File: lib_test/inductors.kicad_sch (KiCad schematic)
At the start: 1 part

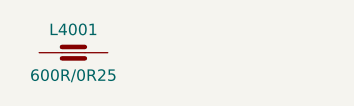
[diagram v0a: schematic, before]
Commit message: Add do not populate parts
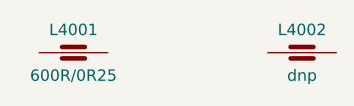
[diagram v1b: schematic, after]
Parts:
- added L4002: dnp, lily_footprints:ind_0805_dnp, symbol lily_symbols:ind_bead_do_not_populate_0805
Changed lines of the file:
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@@
 	(paper "A4")
+	(symbol
+		(lib_id "lily_symbols:ind_bead_do_not_populate_0805")
+		(at 50.8 25.4 0)
+		(unit 1)
+		(exclude_from_sim no)
+		(in_bom yes)
+		(on_board yes)
+		(dnp no)
+		(property "Reference" "L4002"
+			(at 54.61 22.86 0)
+			(effects
+				(font
+					(size 1.27 1.27)
+				)
+			)
+		)
+		(property "Value" "dnp"
+			(at 54.61 27.94 0)
+			(effects
+				(font
+					(size 1.27 1.27)
+				)
+			)
+		)
+		(property "Footprint" "lily_footprints:ind_0805_dnp"
+			(at 54.61 35.56 0)
+			(effects
+				(font
+					(size 1.27 1.27)
+				)
+				(hide yes)
+			)
+		)
+		(property "Datasheet" ""
+			(at 50.8 25.4 0)
+			(effects
+				(font
+					(size 1.27 1.27)
+				)
+				(hide yes)
+			)
+		)
+		(property "Description" ""
+			(at 50.8 25.4 0)
+			(effects
+				(font
+					(size 1.27 1.27)
+				)
+				(hide yes)
+			)
+		)
+		(property "Revision" "1"
+			(at 54.61 30.48 0)
+			(effects
+				(font
+					(size 1.27 1.27)
+				)
+				(hide yes)
+			)
+		)
+		(property "Status" "Active"
+			(at 54.61 33.02 0)
+			(effects
+				(font
+					(size 1.27 1.27)
+				)
+				(hide yes)
+			)
+		)
+		(pin "2"
+		)
+		(pin "1"
+		)
+		(instances
+			(project "kicad_lib_test"
+				(path "/032b8f2d-5c08-4381-9e3a-c197ca84e3c5/ac804940-04be-4885-b738-67220611f5f6"
+					(reference "L4002")
+					(unit 1)
+				)
+			)
+		)
+	)
 	(symbol
 		(lib_id "lily_symbols:ind_bead_600R@100MHz_1A5_0R25_0805")

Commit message: add diode tvs uni 2 channel 12V
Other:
- company: (none) -> LilyTronics
- title: (none) -> Lily KiCad Library test
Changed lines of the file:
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@@
 	(generator_version "8.0")
 	(paper "A4")
+	(title_block
+		(title "Lily KiCad Library test")
+		(date "2024-04-28")
+		(rev "1")
+		(company "LilyTronics")
+	)
 	(symbol
 		(lib_id "lily_symbols:ind_bead_do_not_populate_0805")

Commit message: add check for 3D models
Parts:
- L4002: Status Active -> (none)
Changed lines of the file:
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@@
-			)
-		)
-		(property "Status" "Active"
-			(at 54.61 33.02 0)
-			(effects
-				(font
-					(size 1.27 1.27)
-				)
-				(hide yes)
 			)
 		)

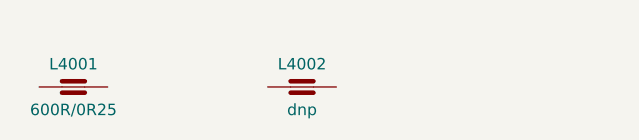
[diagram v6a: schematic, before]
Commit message: add ACM90V
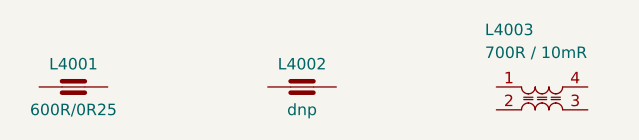
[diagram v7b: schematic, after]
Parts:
- added L4003: 700R / 10mR, lily_footprints:ind_common_mode_9x7mm, symbol lily_symbols:ind_common_mode_700R@100MHz_5A_10mR_9x7mm
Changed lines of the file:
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@@
+	)
+	(symbol
+		(lib_id "lily_symbols:ind_common_mode_700R@100MHz_5A_10mR_9x7mm")
+		(at 76.2 25.4 0)
+		(unit 1)
+		(exclude_from_sim no)
+		(in_bom yes)
+		(on_board yes)
+		(dnp no)
+		(property "Reference" "L4003"
+			(at 74.93 19.05 0)
+			(effects
+				(font
+					(size 1.27 1.27)
+				)
+				(justify left)
+			)
+		)
+		(property "Value" "700R / 10mR"
+			(at 74.93 21.59 0)
+			(effects
+				(font
+					(size 1.27 1.27)
+				)
+				(justify left)
+			)
+		)
+		(property "Footprint" "lily_footprints:ind_common_mode_9x7mm"
+			(at 81.28 35.56 0)
+			(effects
+				(font
+					(size 1.27 1.27)
+				)
+				(hide yes)
+			)
+		)
+		(property "Datasheet" ""
+			(at 76.2 25.4 0)
+			(effects
+				(font
+					(size 1.27 1.27)
+				)
+				(hide yes)
+			)
+		)
+		(property "Description" ""
+			(at 76.2 25.4 0)
+			(effects
+				(font
+					(size 1.27 1.27)
+				)
+				(hide yes)
+			)
+		)
+		(property "Revision" "1"
+			(at 81.28 30.48 0)
+			(effects
+				(font
+					(size 1.27 1.27)
+				)
+				(hide yes)
+			)
+		)
+		(property "Status" "Active"
+			(at 81.28 33.02 0)
+			(effects
+				(font
+					(size 1.27 1.27)
+				)
+				(hide yes)
+			)
+		)
+		(property "Manufacturer" "TDK"
+			(at 81.28 38.1 0)
+			(effects
+				(font
+					(size 1.27 1.27)
+				)
+				(hide yes)
+			)
+		)
+		(property "Manufacturer_ID" "ACM90V-701-2PL-TL00"
+			(at 81.28 40.64 0)
+			(effects
+				(font
+					(size 1.27 1.27)
+				)
+				(hide yes)
+			)
+		)
+		(property "Lily_ID" "1916-10003"
+			(at 81.28 43.18 0)
+			(effects
+				(font
+					(size 1.27 1.27)
+				)
+				(hide yes)
+			)
+		)
+		(property "JLCPCB_ID" "C87510"
+			(at 81.28 45.72 0)
+			(effects
+				(font
+					(size 1.27 1.27)
+				)
+				(hide yes)
+			)
+		)
+		(property "JLCPCB_STATUS" "Extended"
+			(at 81.28 48.26 0)
+			(effects
+				(font
+					(size 1.27 1.27)
+				)
+				(hide yes)
+			)
+		)
+		(pin "2"
+		)
+		(pin "4"
+		)
+		(pin "3"
+		)
+		(pin "1"
+		)
+		(instances
+			(project "kicad_lib_test"
+				(path "/032b8f2d-5c08-4381-9e3a-c197ca84e3c5/ac804940-04be-4885-b738-67220611f5f6"
+					(reference "L4003")
+					(unit 1)
+				)
+			)
+		)
 	)
 	(symbol

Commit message: updated value check for symbols
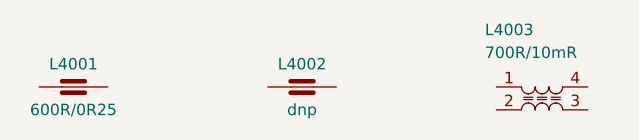
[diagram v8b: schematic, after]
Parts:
- L4003: value 700R / 10mR -> 700R/10mR
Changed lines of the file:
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@@
 			)
 		)
-		(property "Value" "700R / 10mR"
+		(property "Value" "700R/10mR"
 			(at 74.93 21.59 0)
 			(effects
